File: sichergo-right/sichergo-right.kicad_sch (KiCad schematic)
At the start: 26 parts, among them J2 Conn_01x04_Pin, Q1 2N7002, U10 SN74LVC1G125DBV, U7 YTS1C0033BBG01, U8 STM32F103C8Tx, U9 SN74LVC1G125DBV, Y2 Crystal_GND24

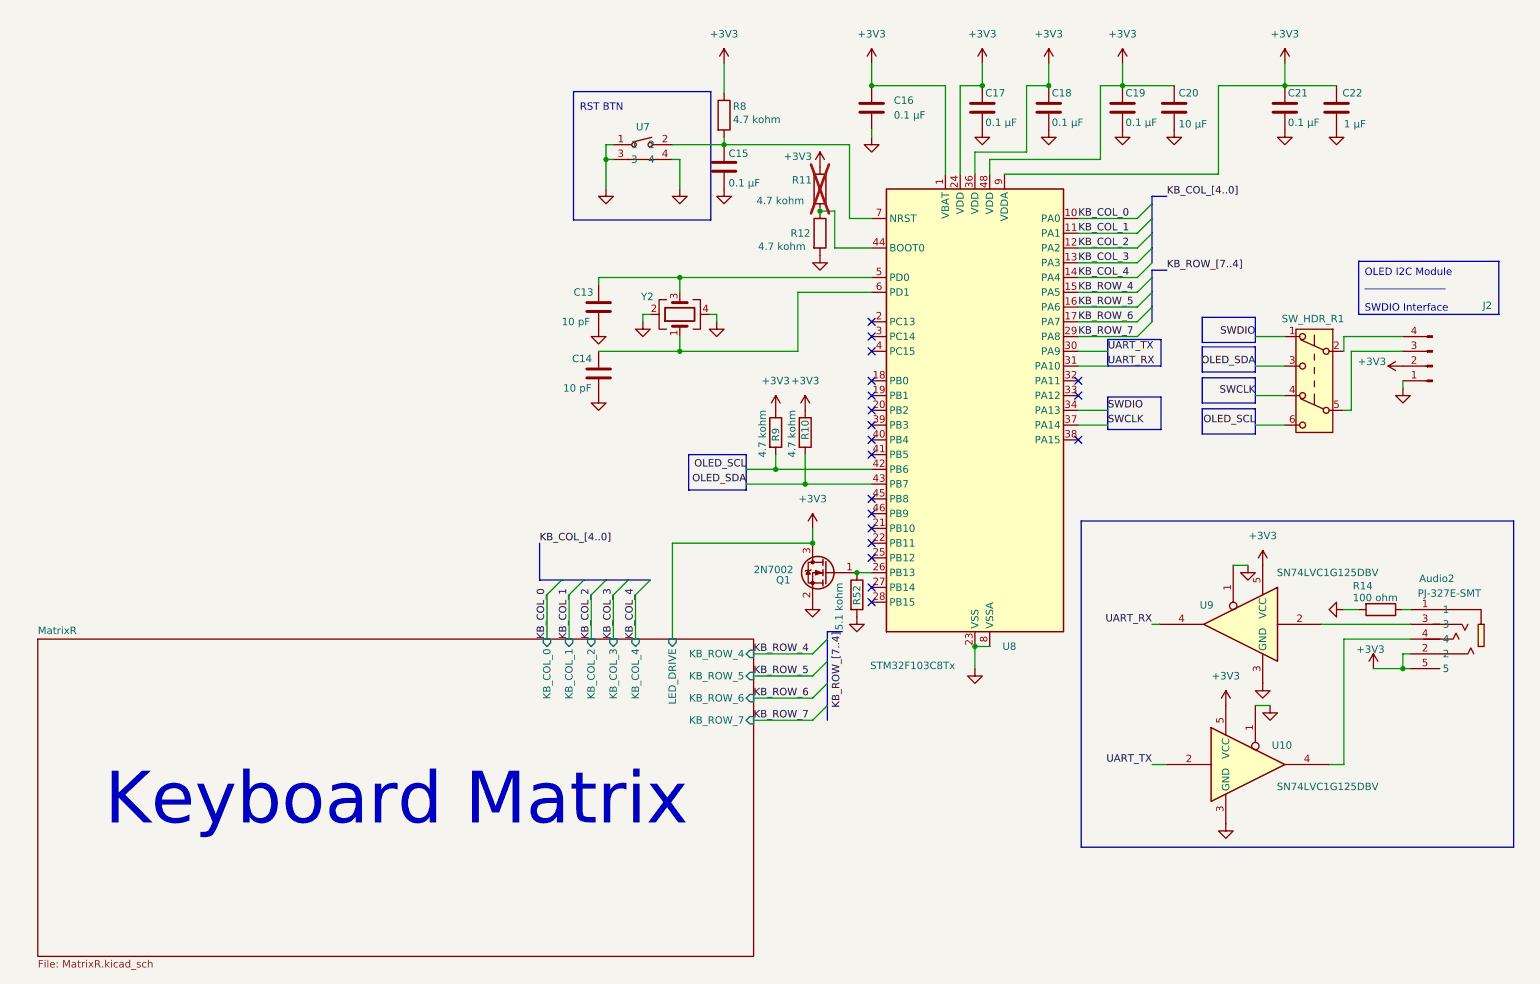
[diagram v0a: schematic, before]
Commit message: Split design in two PCBs and remake layout
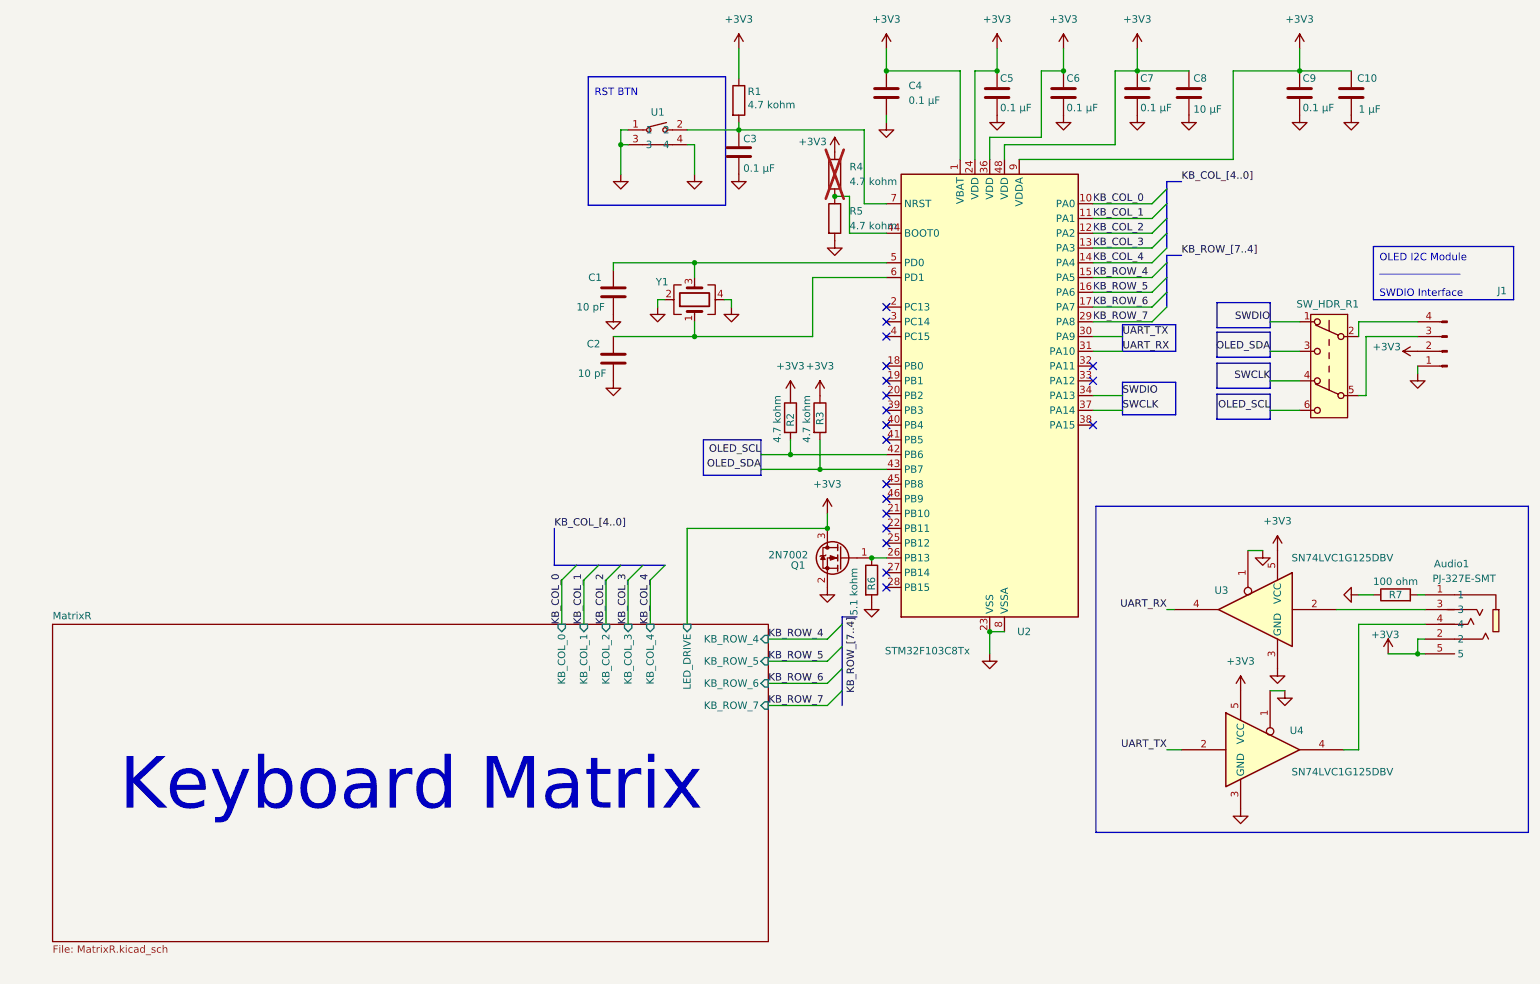
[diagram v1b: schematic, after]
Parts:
- removed Audio2: PJ-327E-SMT, easyeda2kicad:AUDIO-SMD_PJ-327E-SMT, symbol easyeda2kicad:PJ-327E-SMT
- removed C13, C14: 10 pF, 0805 (2012 Metric), symbol #inventree:CL21C100CBANNNC
- removed C15, C16, C17, C18, C19, C21: 0.1 µF, 0805 (2012 Metric), symbol #inventree:CL21B104KBCNNNC
- removed C20: 10 µF, 0805 (2012 Metric), symbol #inventree:CL21A106KOQNNNE
- removed C22: 1 µF, 0805 (2012 Metric), symbol #inventree:CL21B105KAFNNNE
- removed J2: Conn_01x04_Pin, Connector_PinSocket_2.54mm:PinSocket_1x04_P2.54mm_Horizontal, symbol Connector:Conn_01x04_Pin
- removed R10, R9: 4.7 kohm, symbol #inventree:RC0603FR-074K7L
- removed R11, R12: 4.7 kohm, symbol #inventree:ERJ-6GEYJ472V
- removed R14: 100 ohm, Resistor_SMD:R_0805_2012Metric_Pad1.20x1.40mm_HandSolder, symbol #inventree:ERJ-6GEYJ101V
- removed R52: 5.1 kohm, Resistor_SMD:R_0612_1632Metric_Pad1.18x3.40mm_HandSolder, symbol #inventree:RC0603FR-075K1L
- removed R8: 4.7 kohm, Resistor_SMD:R_0603_1608Metric_Pad0.98x0.95mm_HandSolder, symbol #inventree:RC0603FR-074K7L
- removed U10, U9: SN74LVC1G125DBV, Package_TO_SOT_SMD:SOT-23-5_HandSoldering, symbol 74xGxx:SN74LVC1G125DBV
- removed U7: YTS1C0033BBG01, easyeda2kicad:SW-SMD_YIYUAN_YTS1C003XXX, symbol easyeda2kicad:YTS1C0033BBG01
- removed U8: STM32F103C8Tx, Package_QFP:LQFP-48_7x7mm_P0.5mm, symbol MCU_ST_STM32F1:STM32F103C8Tx
- removed Y2: Crystal_GND24, Crystal:Crystal_SMD_3225-4Pin_3.2x2.5mm_HandSoldering, symbol Device:Crystal_GND24
- added Audio1: PJ-327E-SMT, easyeda2kicad:AUDIO-SMD_PJ-327E-SMT, symbol easyeda2kicad:PJ-327E-SMT
- added C1, C2: 10 pF, 0805 (2012 Metric), symbol #inventree:CL21C100CBANNNC
- added C10: 1 µF, 0805 (2012 Metric), symbol #inventree:CL21B105KAFNNNE
- added C3, C4, C5, C6, C7, C9: 0.1 µF, 0805 (2012 Metric), symbol #inventree:CL21B104KBCNNNC
- added C8: 10 µF, 0805 (2012 Metric), symbol #inventree:CL21A106KOQNNNE
- added J1: Conn_01x04_Pin, Connector_PinSocket_2.54mm:PinSocket_1x04_P2.54mm_Horizontal, symbol Connector:Conn_01x04_Pin
- added R1, R4, R5: 4.7 kohm, Resistor_SMD:R_0603_1608Metric_Pad0.98x0.95mm_HandSolder, symbol #inventree:RC0603FR-074K7L
- added R2, R3: 4.7 kohm, symbol #inventree:RC0603FR-074K7L
- added R6: 5.1 kohm, Resistor_SMD:R_0612_1632Metric_Pad1.18x3.40mm_HandSolder, symbol #inventree:RC0603FR-075K1L
- added R7: 100 ohm, Resistor_SMD:R_0603_1608Metric_Pad0.98x0.95mm_HandSolder, symbol #inventree:RC0603FR-07100RL
- added U1: YTS1C0033BBG01, easyeda2kicad:SW-SMD_YIYUAN_YTS1C003XXX, symbol easyeda2kicad:YTS1C0033BBG01
- added U2: STM32F103C8Tx, Package_QFP:LQFP-48_7x7mm_P0.5mm, symbol MCU_ST_STM32F1:STM32F103C8Tx
- added U3, U4: SN74LVC1G125DBV, Package_TO_SOT_SMD:SOT-23-5_HandSoldering, symbol 74xGxx:SN74LVC1G125DBV
- added Y1: Crystal_GND24, Crystal:Crystal_SMD_3225-4Pin_3.2x2.5mm_HandSoldering, symbol Device:Crystal_GND24
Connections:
- net +3V3: now also Audio1.2, Audio1.5, C10.1, C4.1, C5.1, C6.1, C7.1, C8.1, C9.1, J1.2 (Pin_2), R1.1, R2.1, R3.1, R4.1, U2.1 (VBAT), U2.24 (VDD), U2.36 (VDD), U2.48 (VDD), U2.9 (VDDA), U3.5 (VCC), U4.5 (VCC)
- net GND: now also C1.2, C10.2, C2.2, C3.2, C4.2, C5.2, C6.2, C7.2, C8.2, C9.2, J1.1 (Pin_1), R5.2, R6.2, R7.1, U1.1, U1.3, U1.4, U2.23 (VSS), U2.35 (VSS), U2.47 (VSS), U2.8 (VSSA), U3.1, U3.3 (GND), U4.1, U4.3 (GND), Y1.2, Y1.4
- net KB_COL_0: now also U2.10 (PA0)
- net KB_COL_1: now also U2.11 (PA1)
- net KB_COL_2: now also U2.12 (PA2)
- net KB_COL_3: now also U2.13 (PA3)
- net KB_COL_4: now also U2.14 (PA4)
- net KB_ROW_4: now also U2.15 (PA5)
- net KB_ROW_5: now also U2.16 (PA6)
- net KB_ROW_6: now also U2.17 (PA7)
- net KB_ROW_7: now also U2.29 (PA8)
- net OLED_SCL: now also R2.2, U2.42 (PB6)
- net OLED_SDA: now also R3.2, U2.43 (PB7)
- net SWCLK: now also U2.37 (PA14)
- net SWDIO: now also U2.34 (PA13)
- net UART_RX: now also U2.31 (PA10), U3.4
- net UART_TX: now also U2.30 (PA9), U4.2
- net at Q1.1 (G): now also R6.1, U2.26 (PB13)
- net at SW_HDR_R1.2 (B): now also J1.4 (Pin_4)
- net at SW_HDR_R1.5 (B): now also J1.3 (Pin_3)
- new net: C1.1, U2.5 (PD0), Y1.3
- new net: R4.2, R5.1, U2.44 (BOOT0)
- new net: C2.1, U2.6 (PD1), Y1.1
- new net: C3.1, R1.2, U1.2, U2.7 (NRST)
- new net: Audio1.3, U3.2
- new net: Audio1.1, R7.2
- new net: Audio1.4, U4.4

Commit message: Remake entire shape
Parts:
- removed C1, C2: 10 pF, 0805 (2012 Metric), symbol #inventree:CL21C100CBANNNC
- removed C10: 1 µF, 0805 (2012 Metric), symbol #inventree:CL21B105KAFNNNE
- removed C3, C4, C5, C6, C7, C9: 0.1 µF, 0805 (2012 Metric), symbol #inventree:CL21B104KBCNNNC
- removed C8: 10 µF, 0805 (2012 Metric), symbol #inventree:CL21A106KOQNNNE
- removed J1: Conn_01x04_Pin, Connector_PinSocket_2.54mm:PinSocket_1x04_P2.54mm_Horizontal, symbol Connector:Conn_01x04_Pin
- removed Q1: 2N7002, Package_TO_SOT_SMD:SOT-23_Handsoldering, symbol Transistor_FET:2N7002
- removed R1, R4, R5: 4.7 kohm, Resistor_SMD:R_0603_1608Metric_Pad0.98x0.95mm_HandSolder, symbol #inventree:RC0603FR-074K7L
- removed R2, R3: 4.7 kohm, symbol #inventree:RC0603FR-074K7L
- removed R6: 5.1 kohm, Resistor_SMD:R_0612_1632Metric_Pad1.18x3.40mm_HandSolder, symbol #inventree:RC0603FR-075K1L
- removed SW_HDR_R1: SW_Push_DPDT, symbol Switch:SW_Push_DPDT
- removed U1: YTS1C0033BBG01, easyeda2kicad:SW-SMD_YIYUAN_YTS1C003XXX, symbol easyeda2kicad:YTS1C0033BBG01
- removed U2: STM32F103C8Tx, Package_QFP:LQFP-48_7x7mm_P0.5mm, symbol MCU_ST_STM32F1:STM32F103C8Tx
- removed Y1: Crystal_GND24, Crystal:Crystal_SMD_3225-4Pin_3.2x2.5mm_HandSoldering, symbol Device:Crystal_GND24
- added C14, C15: 10 pF, Capacitor_SMD:C_0805_2012Metric_Pad1.18x1.45mm_HandSolder, symbol #inventree:CL21C100CBANNNC
- added C16, C17, C18, C19, C20, C22: 0.1 µF, Capacitor_SMD:C_0805_2012Metric_Pad1.18x1.45mm_HandSolder, symbol #inventree:CL21B104KBCNNNC
- added C21: 10 µF, Capacitor_SMD:C_0805_2012Metric_Pad1.18x1.45mm_HandSolder, symbol #inventree:CL21A106KOQNNNE
- added C23: 1 µF, Capacitor_SMD:C_0805_2012Metric_Pad1.18x1.45mm_HandSolder, symbol #inventree:CL21B105KAFNNNE
- added J2: Conn_01x04_Pin, Connector_PinSocket_2.54mm:PinSocket_1x04_P2.54mm_Horizontal, symbol Connector:Conn_01x04_Pin
- added Q2: 2N7002, Package_TO_SOT_SMD:SOT-23_Handsoldering, symbol Transistor_FET:2N7002
- added R29, R30, R31, R32, R33, R34: 4.7 kohm, Resistor_SMD:R_0603_1608Metric_Pad0.98x0.95mm_HandSolder, symbol #inventree:RC0603FR-074K7L
- added R35: 5.1 kohm, Resistor_SMD:R_0603_1608Metric_Pad0.98x0.95mm_HandSolder, symbol #inventree:RC0603FR-075K1L
- added SW19: MS-22C01-G010, easyeda2kicad:SW-SMD_6P-L7.2-W3.5-P2.50-LS6.0-TL, symbol easyeda2kicad:MS-22C01-G010
- added TP4: TestPoint, TestPoint:TestPoint_THTPad_1.0x1.0mm_Drill0.5mm, symbol Connector:TestPoint
- added U7: YTS1C0033BBG01, easyeda2kicad:SW-SMD_YIYUAN_YTS1C003XXX, symbol easyeda2kicad:YTS1C0033BBG01
- added U8: STM32F103C8Tx, Package_QFP:LQFP-48_7x7mm_P0.5mm, symbol MCU_ST_STM32F1:STM32F103C8Tx
- added Y2: Crystal_GND24, Crystal:Crystal_SMD_3225-4Pin_3.2x2.5mm_HandSoldering, symbol Device:Crystal_GND24
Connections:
- net +3V3: now also C17.1, C18.1, C19.1, C20.1, C21.1, C22.1, C23.1, J2.2 (Pin_2), R29.1, R30.1, R31.1, R32.1, R34.2, U8.1 (VBAT), U8.24 (VDD), U8.36 (VDD), U8.48 (VDD), U8.9 (VDDA)
- net GND: now also C14.2, C15.2, C16.2, C17.2, C18.2, C19.2, C20.2, C21.2, C22.2, C23.2, J2.1 (Pin_1), Q2.2 (S), R33.2, R35.2, U7.1, U7.3, U7.4, U8.23 (VSS), U8.35 (VSS), U8.47 (VSS), U8.8 (VSSA), Y2.2, Y2.4
- net KB_COL_0: now also U8.15 (PA5)
- net KB_COL_1: now also U8.16 (PA6)
- net KB_COL_2: now also U8.17 (PA7)
- net KB_COL_3: now also U8.13 (PA3)
- net KB_COL_4: now also U8.14 (PA4)
- net OLED_SCL: now also R29.2, SW19.3, U8.42 (PB6)
- net OLED_SDA: now also R31.2, SW19.6, U8.43 (PB7)
- net SWCLK: now also SW19.1, U8.37 (PA14)
- net SWDIO: now also SW19.4, U8.34 (PA13)
- net UART_RX: now also U8.31 (PA10)
- net UART_TX: now also U8.30 (PA9)
- new net: J2.3 (Pin_3), SW19.2
- new net: J2.4 (Pin_4), SW19.5
- new net: Q2.1 (G), R35.1, U8.26 (PB13)
- new net: R32.2, R33.1, U8.44 (BOOT0)
- new net: C14.1, U8.5 (PD0), Y2.3
- new net: C15.1, U8.6 (PD1), Y2.1
- new net: C16.1, R30.2, U7.2, U8.7 (NRST)
- new net D+: U8.33 (PA12)
- new net D-: U8.32 (PA11)
- new net KB_ROW_0: U8.38 (PA15)
- new net KB_ROW_1: U8.39 (PB3)
- new net KB_ROW_2: U8.40 (PB4)
- new net KB_ROW_3: U8.41 (PB5)
- new net MatrixR/LED_DRIVE: Q2.3 (D), R34.1, TP4.1
- no-connect marks 19 -> 17
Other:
- sheet MatrixR ports: added KB_ROW_0, KB_ROW_1, KB_ROW_2, KB_ROW_3; removed KB_ROW_4, KB_ROW_5, KB_ROW_6, KB_ROW_7
- moved on the sheet: Audio1, R7, U3, U4

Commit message: Fix keyboard layout size
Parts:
- removed C14, C15: 10 pF, Capacitor_SMD:C_0805_2012Metric_Pad1.18x1.45mm_HandSolder, symbol #inventree:CL21C100CBANNNC
- removed C16, C17, C18, C19, C20, C22: 0.1 µF, Capacitor_SMD:C_0805_2012Metric_Pad1.18x1.45mm_HandSolder, symbol #inventree:CL21B104KBCNNNC
- removed C21: 10 µF, Capacitor_SMD:C_0805_2012Metric_Pad1.18x1.45mm_HandSolder, symbol #inventree:CL21A106KOQNNNE
- removed C23: 1 µF, Capacitor_SMD:C_0805_2012Metric_Pad1.18x1.45mm_HandSolder, symbol #inventree:CL21B105KAFNNNE
- removed J2: Conn_01x04_Pin, Connector_PinSocket_2.54mm:PinSocket_1x04_P2.54mm_Horizontal, symbol Connector:Conn_01x04_Pin
- removed Q2: 2N7002, Package_TO_SOT_SMD:SOT-23_Handsoldering, symbol Transistor_FET:2N7002
- removed R29, R30, R31, R32, R33, R34: 4.7 kohm, Resistor_SMD:R_0603_1608Metric_Pad0.98x0.95mm_HandSolder, symbol #inventree:RC0603FR-074K7L
- removed R35: 5.1 kohm, Resistor_SMD:R_0603_1608Metric_Pad0.98x0.95mm_HandSolder, symbol #inventree:RC0603FR-075K1L
- removed SW19: MS-22C01-G010, easyeda2kicad:SW-SMD_6P-L7.2-W3.5-P2.50-LS6.0-TL, symbol easyeda2kicad:MS-22C01-G010
- removed TP4: TestPoint, TestPoint:TestPoint_THTPad_1.0x1.0mm_Drill0.5mm, symbol Connector:TestPoint
- removed U7: YTS1C0033BBG01, easyeda2kicad:SW-SMD_YIYUAN_YTS1C003XXX, symbol easyeda2kicad:YTS1C0033BBG01
- removed U8: STM32F103C8Tx, Package_QFP:LQFP-48_7x7mm_P0.5mm, symbol MCU_ST_STM32F1:STM32F103C8Tx
- removed Y2: Crystal_GND24, Crystal:Crystal_SMD_3225-4Pin_3.2x2.5mm_HandSoldering, symbol Device:Crystal_GND24
- added C1, C2: 10 pF, Capacitor_SMD:C_0805_2012Metric_Pad1.18x1.45mm_HandSolder, symbol #inventree:CL21C100CBANNNC
- added C10: 1 µF, Capacitor_SMD:C_0805_2012Metric_Pad1.18x1.45mm_HandSolder, symbol #inventree:CL21B105KAFNNNE
- added C3, C4, C5, C6, C7, C9: 0.1 µF, Capacitor_SMD:C_0805_2012Metric_Pad1.18x1.45mm_HandSolder, symbol #inventree:CL21B104KBCNNNC
- added C8: 10 µF, Capacitor_SMD:C_0805_2012Metric_Pad1.18x1.45mm_HandSolder, symbol #inventree:CL21A106KOQNNNE
- added J1: Conn_01x04_Pin, Connector_PinSocket_2.54mm:PinSocket_1x04_P2.54mm_Horizontal, symbol Connector:Conn_01x04_Pin
- added Q1: 2N7002, Package_TO_SOT_SMD:SOT-23_Handsoldering, symbol Transistor_FET:2N7002
- added R1, R2, R3, R4, R5, R6: 4.7 kohm, Resistor_SMD:R_0603_1608Metric_Pad0.98x0.95mm_HandSolder, symbol #inventree:RC0603FR-074K7L
- added R7: 5.1 kohm, Resistor_SMD:R_0603_1608Metric_Pad0.98x0.95mm_HandSolder, symbol #inventree:RC0603FR-075K1L
- added SW1: MS-22C01-G010, easyeda2kicad:SW-SMD_6P-L7.2-W3.5-P2.50-LS6.0-TL, symbol easyeda2kicad:MS-22C01-G010
- added TP1: TestPoint, TestPoint:TestPoint_THTPad_1.0x1.0mm_Drill0.5mm, symbol Connector:TestPoint
- added U1: YTS1C0033BBG01, easyeda2kicad:SW-SMD_YIYUAN_YTS1C003XXX, symbol easyeda2kicad:YTS1C0033BBG01
- added U2: STM32F103C8Tx, Package_QFP:LQFP-48_7x7mm_P0.5mm, symbol MCU_ST_STM32F1:STM32F103C8Tx
- added Y1: Crystal_GND24, Crystal:Crystal_SMD_3225-4Pin_3.2x2.5mm_HandSoldering, symbol Device:Crystal_GND24
- renumbered R7 to R8
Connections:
- net +3V3: now also C10.1, C4.1, C5.1, C6.1, C7.1, C8.1, C9.1, J1.2 (Pin_2), R1.1, R2.1, R3.1, R4.1, R5.1, U2.1 (VBAT), U2.24 (VDD), U2.36 (VDD), U2.48 (VDD), U2.9 (VDDA)
- net D+: now also U2.33 (PA12)
- net D-: now also U2.32 (PA11)
- net GND: now also C1.2, C10.2, C2.2, C3.2, C4.2, C5.2, C6.2, C7.2, C8.2, C9.2, J1.1 (Pin_1), Q1.2 (S), R6.2, R7.2, U1.1, U1.3, U1.4, U2.23 (VSS), U2.35 (VSS), U2.47 (VSS), U2.8 (VSSA), Y1.2, Y1.4
- net KB_COL_0: now also U2.15 (PA5)
- net KB_COL_1: now also U2.16 (PA6)
- net KB_COL_2: now also U2.17 (PA7)
- net KB_COL_3: now also U2.13 (PA3)
- net KB_COL_4: now also U2.14 (PA4)
- net KB_ROW_0: now also U2.21 (PB10)
- net KB_ROW_1: now also U2.18 (PB0)
- net KB_ROW_2: now also U2.19 (PB1)
- net KB_ROW_3: now also U2.20 (PB2)
- net MatrixR/LED_DRIVE: now also Q1.3 (D), R4.2, TP1.1
- net OLED_SCL: now also R1.2, SW1.3, U2.42 (PB6)
- net OLED_SDA: now also R3.2, SW1.6, U2.43 (PB7)
- net SWCLK: now also SW1.1, U2.37 (PA14)
- net SWDIO: now also SW1.4, U2.34 (PA13)
- net UART_RX: now also U2.31 (PA10)
- net UART_TX: now also U2.30 (PA9)
- new net: C3.1, R2.2, U1.2, U2.7 (NRST)
- new net: R5.2, R6.1, U2.44 (BOOT0)
- new net: J1.3 (Pin_3), SW1.2
- new net: J1.4 (Pin_4), SW1.5
- new net: Q1.1 (G), R7.1, U2.26 (PB13)
- new net: C1.1, U2.5 (PD0), Y1.3
- new net: C2.1, U2.6 (PD1), Y1.1
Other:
- moved on the sheet: Audio1, R8, U3, U4

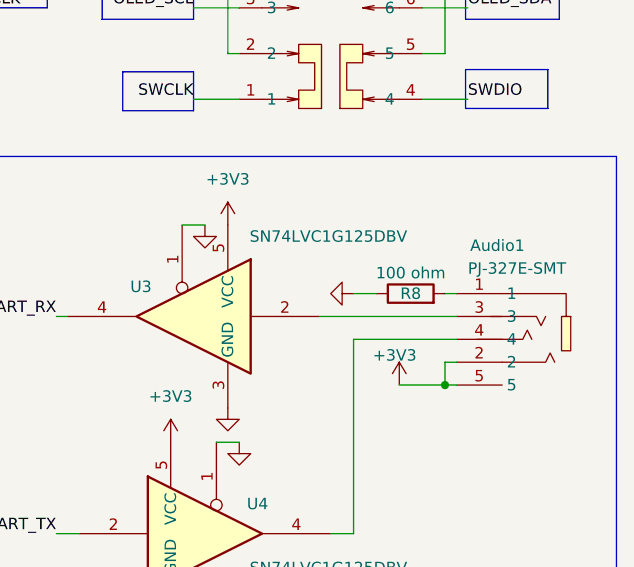
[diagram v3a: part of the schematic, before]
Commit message: Start placement of right side
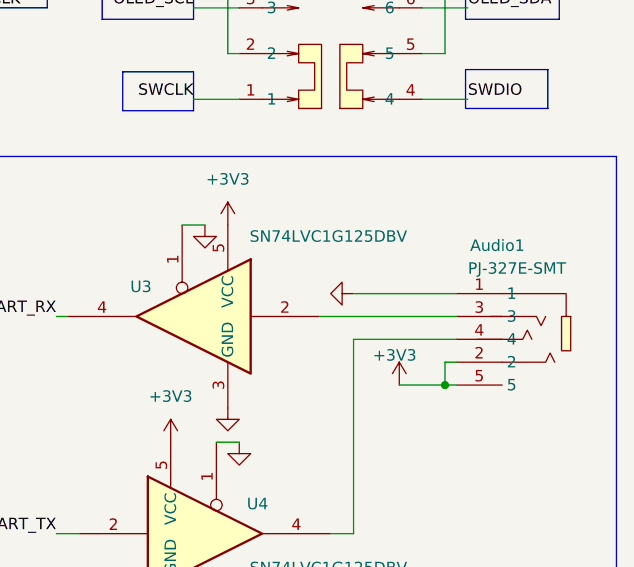
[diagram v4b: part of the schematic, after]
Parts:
- removed R8: 100 ohm, Resistor_SMD:R_0603_1608Metric_Pad0.98x0.95mm_HandSolder, symbol #inventree:RC0603FR-07100RL
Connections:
- net GND: now also Audio1.1
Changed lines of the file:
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@@
 	(wire
 		(pts
-			(xy 264.16 123.19) (xy 265.43 123.19)
-		)
-		(stroke
-			(width 0)
-			(type default)
-		)
-	)
-	(wire
-		(pts
 			(xy 196.85 44.45) (xy 196.85 33.02)
 		)
@@
 	(wire
 		(pts
-			(xy 254 123.19) (xy 256.54 123.19)
+			(xy 254 123.19) (xy 265.43 123.19)
 		)
 		(stroke
@@
 					(unit 1)
 				)
-			)
-		)
-	)
-	(symbol
-		(lib_id "#inventree:RC0603FR-07100RL")
-		(at 260.35 123.19 90)
-		(unit 1)
-		(exclude_from_sim no)
-		(in_bom yes)
-		(on_board yes)
-		(dnp no)
-		(property "Reference" "R8"
-			(at 260.35 123.19 90)
-			(effects
-				(font
-					(size 1.27 1.27)
-				)
-			)
-		)
-		(property "Value" "100 ohm"
-			(at 260.35 120.904 90)
-			(effects
-				(font
-					(size 1.27 1.27)
-				)
-			)
-		)
-		(property "Footprint" "Resistor_SMD:R_0603_1608Metric_Pad0.98x0.95mm_HandSolder"
-			(at 260.35 124.968 90)
-			(effects
-				(font
-					(size 1.27 1.27)
-				)
-				(hide yes)
-			)
-		)
-		(property "Datasheet" "http://10.0.0.41/media/attachments/part/71/PYu-RC_Group_51_RoHS_L_12.pdf"
-			(at 260.35 123.19 0)
-			(effects
-				(font
-					(size 1.27 1.27)
-				)
-				(hide yes)
-			)
-		)
-		(property "Description" "RES 100 OHM 1% 1/10W 0603"
-			(at 260.35 123.19 0)
-			(effects
-				(font
-					(size 1.27 1.27)
-				)
-				(hide yes)
-			)
-		)
-		(property "InvenTree" "71"
-			(at 260.35 123.19 0)
-			(effects
-				(font
-					(size 1.27 1.27)
-				)
-				(hide yes)
-			)
-		)
-		(property "Mounting Type" "0603"
-			(at 260.35 123.19 0)
-			(effects
-				(font
-					(size 1.27 1.27)
-				)
-				(hide yes)
-			)
-		)
-		(property "Package Type" "0603 (1608 Metric)"
-			(at 260.35 123.19 0)
-			(effects
-				(font
-					(size 1.27 1.27)
-				)
-				(hide yes)
-			)
-		)
-		(property "Part URL" "http://10.0.0.41:7333/part/71/"
-			(at 260.35 123.19 0)
-			(effects
-				(font
-					(size 1.27 1.27)
-				)
-				(hide yes)
-			)
-		)
-		(property "Rated Power" "0.1W, 1/10W"
-			(at 260.35 123.19 0)
-			(effects
-				(font
-					(size 1.27 1.27)
-				)
-				(hide yes)
-			)
-		)
-		(property "Tolerance" "1%"
-			(at 260.35 123.19 0)
-			(effects
-				(font
-					(size 1.27 1.27)
-				)
-				(hide yes)
-			)
-		)
-		(pin "2"
-		)
-		(pin "1"
-		)
-		(instances
-			(project ""
-				(path "/7d6715fb-1e77-4b7f-bc05-ec156d7f2ccd"
-					(reference "R8")
-					(unit 1)
-				)
